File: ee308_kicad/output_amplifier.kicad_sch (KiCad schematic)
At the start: 24 parts, among them Q2 2N3904, Q4 2N3904, Q5 2N3904, Q6 2N3906, Q7 2N3904, Q8 2N3906

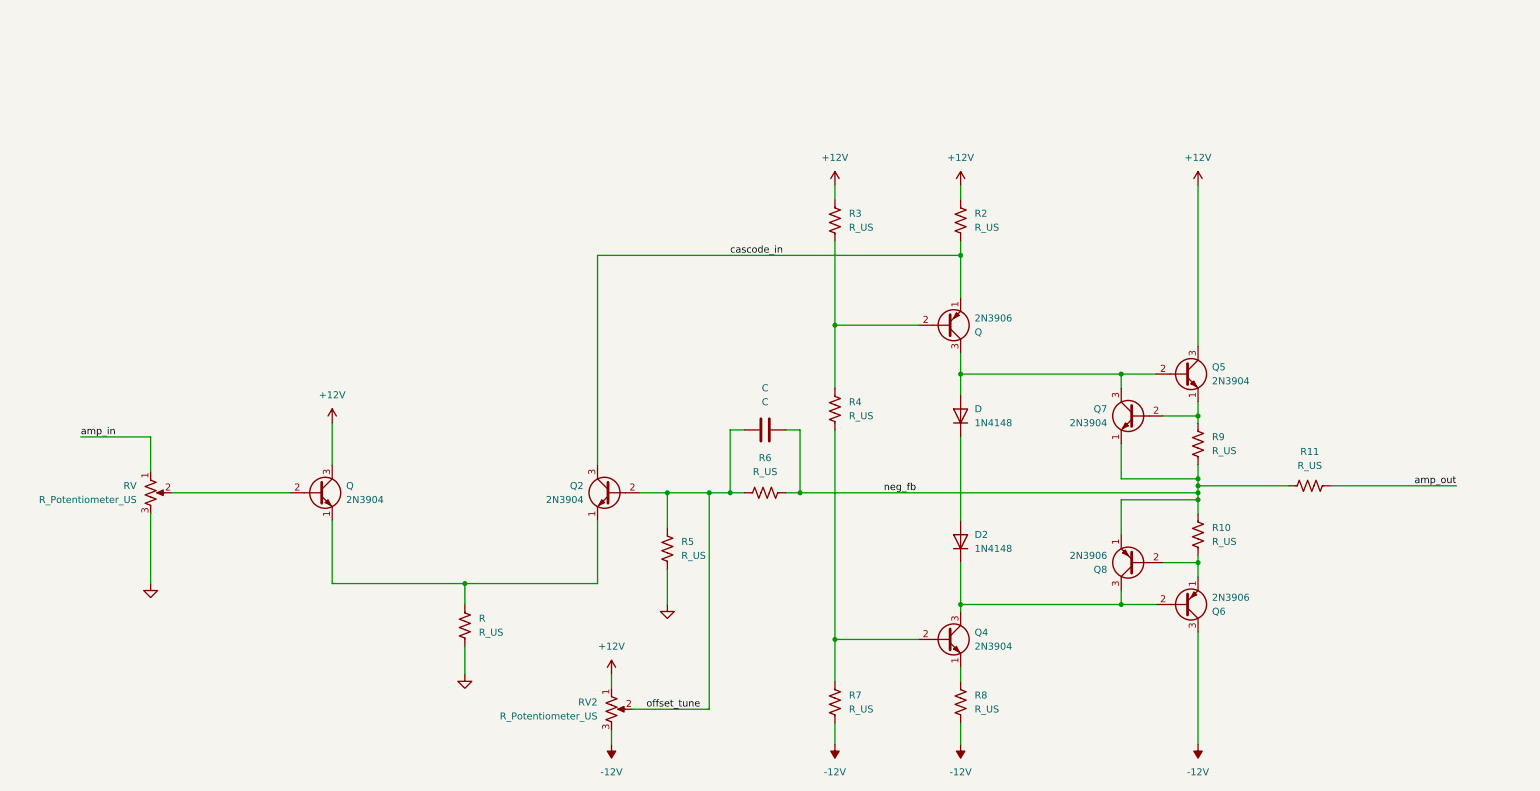
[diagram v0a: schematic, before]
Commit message: Update amplifier sims and kicad schematic.
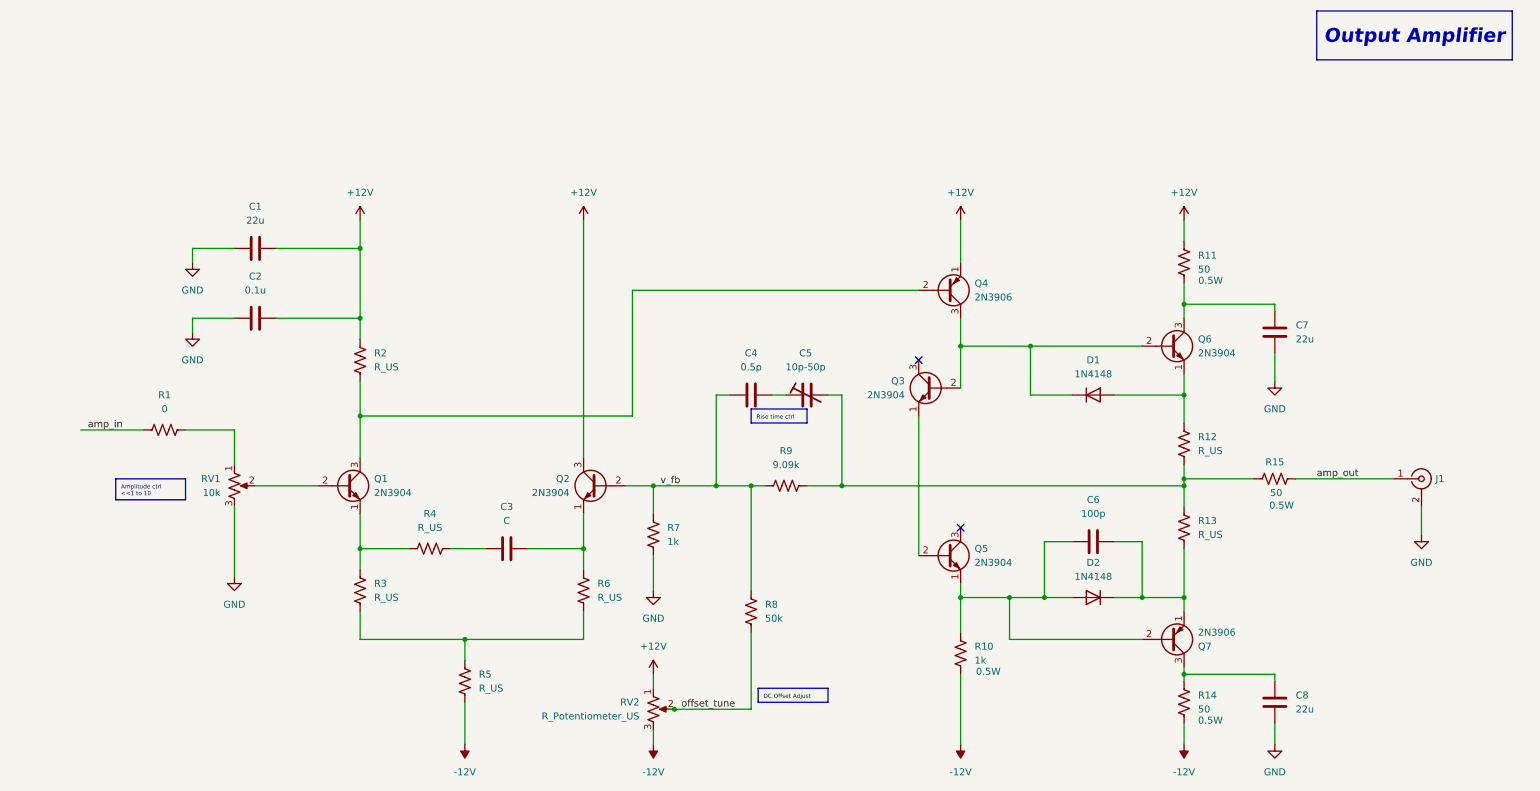
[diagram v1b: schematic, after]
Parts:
- removed C: C, symbol Device:C
- removed Q4, Q7: 2N3904, Package_TO_SOT_THT:TO-92_Inline, symbol Transistor_BJT:2N3904
- removed Q8: 2N3906, Package_TO_SOT_THT:TO-92_Inline, symbol Transistor_BJT:2N3906
- removed R5: R_US, symbol Device:R_US
- added C1, C7, C8: 22u, Capacitor_SMD:C_0805_2012Metric_Pad1.18x1.45mm_HandSolder, symbol Device:C
- added C2: 0.1u, Capacitor_SMD:C_0805_2012Metric_Pad1.18x1.45mm_HandSolder, symbol Device:C
- added C3: C, Capacitor_SMD:C_0805_2012Metric_Pad1.18x1.45mm_HandSolder, symbol Device:C
- added C4: 0.5p, Capacitor_SMD:C_0805_2012Metric_Pad1.18x1.45mm_HandSolder, symbol Device:C
- added C5: 10p-50p, Capacitor_SMD:C_Trimmer_Murata_TZY2, symbol Device:C_Trim
- added C6: 100p, Capacitor_SMD:C_0805_2012Metric_Pad1.18x1.45mm_HandSolder, symbol Device:C
- added J1: Conn_Coaxial, Connector_Coaxial:BNC_TEConnectivity_1478035_Horizontal, symbol Connector:Conn_Coaxial
- added Q3, Q5: 2N3904, Package_TO_SOT_THT:TO-92_Inline, symbol Transistor_BJT:2N3904
- added R1: 0, Resistor_SMD:R_0805_2012Metric_Pad1.20x1.40mm_HandSolder, symbol Device:R_US
- added R12, R13: R_US, Resistor_SMD:R_0805_2012Metric_Pad1.20x1.40mm_HandSolder, symbol Device:R_US
- added R14, R15: 50, Resistor_SMD:R_1206_3216Metric_Pad1.30x1.75mm_HandSolder, symbol Device:R_US
- R10: value R_US -> 1k; footprint (none) -> Resistor_SMD:R_1206_3216Metric_Pad1.30x1.75mm_HandSolder; Power (none) -> 0.5W
- R11: value R_US -> 50; footprint (none) -> Resistor_SMD:R_1206_3216Metric_Pad1.30x1.75mm_HandSolder; Power (none) -> 0.5W
- R2, R3, R4, R6: footprint (none) -> Resistor_SMD:R_0805_2012Metric_Pad1.20x1.40mm_HandSolder
- R7: value R_US -> 1k; footprint (none) -> Resistor_SMD:R_0805_2012Metric_Pad1.20x1.40mm_HandSolder
- R8: value R_US -> 50k; footprint (none) -> Resistor_SMD:R_0805_2012Metric_Pad1.20x1.40mm_HandSolder
- R9: value R_US -> 9.09k; footprint (none) -> Resistor_SMD:R_0805_2012Metric_Pad1.20x1.40mm_HandSolder
- RV1: renamed from RV; value R_Potentiometer_US -> 10k; footprint (none) -> Potentiometer_SMD:Potentiometer_ACP_CA6-VSMD_Vertical
- renumbered D to D1, Q to Q1, Q to Q4, Q5 to Q6, Q6 to Q7, R to R5
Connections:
- net +12V: now also Q2.3 (C), Q4.1 (E), R11.1, C1.2, C2.2; no longer Q1.3 (C), Q6.3 (C), R3.1
- net -12V: now also R10.2, R5.2, R14.2; no longer Q7.3 (C), R7.2, R8.2
- net GND: now also R7.2, C1.1, C2.1, C7.1, C8.1, J1.2 (Ext); no longer R5.2
- net amp_in: now also R1.2; no longer RV1.1
- net amp_out: now also J1.1 (In), R15.2; no longer R11.2
- net offset_tune: now also R8.2; no longer Q2.2 (B), R6.1
- net at D1.1 (K): now also Q4.3 (C), Q6.2 (B), Q3.2 (B); no longer D2.2 (A)
- net at Q7.1 (E): now also D2.1 (K), C6.2, R13.2; no longer R10.2
- net v_fb: now reaches R8.1
- net v_fb: now also Q2.2 (B), R7.1, R9.2, C4.1
- net at Q6.1 (E): now also D1.2 (A), R12.1; no longer R9.1
- net at Q7.2 (B): now also D2.2 (A), R10.1, C6.1, Q5.1 (E); no longer D2.1 (K)
- net at R4.2: now also Q1.1 (E), R3.1; no longer R7.1
- removed net cascode_in: Q2.3 (C), Q4.1 (E), R2.2
- removed net neg_fb: R10.1, R11.1, R6.2, R9.2
- new net: C7.2, Q6.3 (C), R11.2
- new net: C3.1, R4.1
- new net: Q3.1 (E), Q5.2 (B)
- new net: Q1.3 (C), Q4.2 (B), R2.2
- new net: C3.2, Q2.1 (E), R6.1
- new net: R3.2, R5.1, R6.2
- new net: C4.2, C5.1
- new net: C5.2, R12.2, R13.1, R15.1, R9.1
- new net: R1.1, RV1.1
- new net: C8.2, Q7.3 (C), R14.1
- no-connect marks 0 -> 2
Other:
- moved on the sheet: D1, D2, Q1, Q2, Q4, Q6, Q7, R5, RV1, RV2

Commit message: Update amplifier sims and kicad schematic.
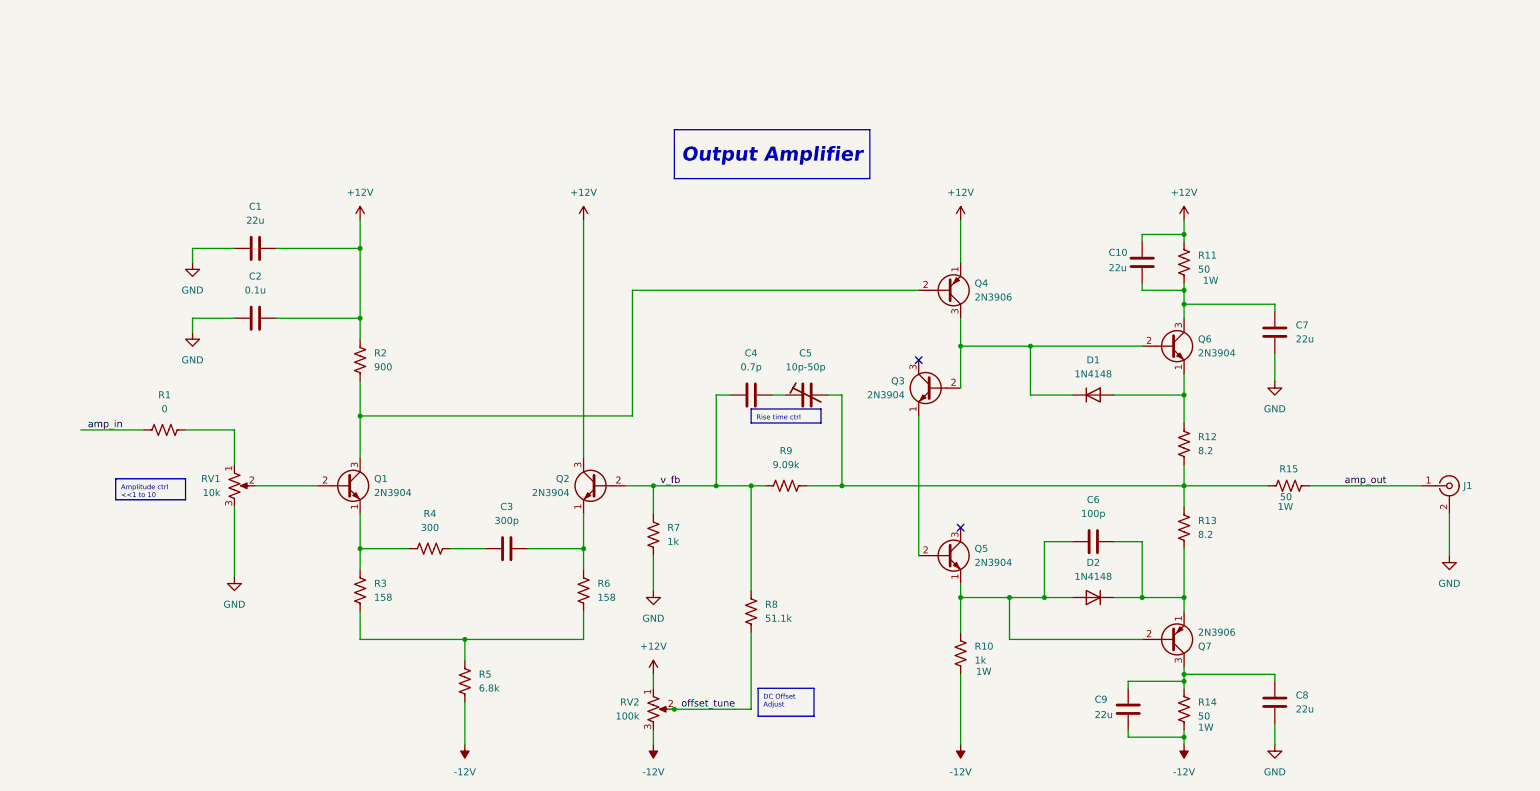
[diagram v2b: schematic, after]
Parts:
- added C10, C9: 22u, Capacitor_SMD:C_0805_2012Metric_Pad1.18x1.45mm_HandSolder, symbol Device:C
- C3: value C -> 300p
- C4: value 0.5p -> 0.7p
- R10, R11, R14, R15: Power 0.5W -> 1W
- R12, R13: value R_US -> 8.2
- R2: value R_US -> 900
- R3, R6: value R_US -> 158
- R4: value R_US -> 300
- R5: value R_US -> 6.8k; footprint (none) -> Resistor_SMD:R_1206_3216Metric_Pad1.30x1.75mm_HandSolder
- R8: value 50k -> 51.1k
- RV2: value R_Potentiometer_US -> 100k
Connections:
- net +12V: now also C10.2
- net -12V: now also C9.1
- net at C7.2, Q6.3 (C), R11.2: now also C10.1
- net at C8.2, Q7.3 (C), R14.1: now also C9.2
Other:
- moved on the sheet: J1, R14, R15

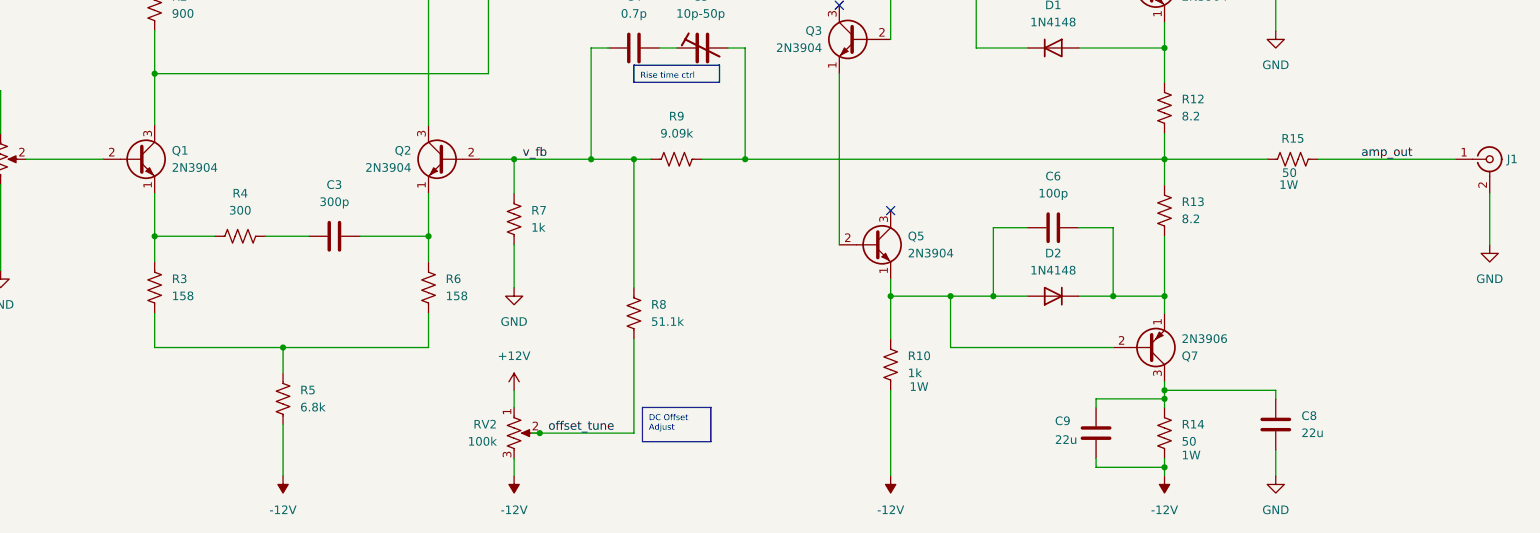
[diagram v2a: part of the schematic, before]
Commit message: Add initial Schmitt trigger simulation with working square wave outputs.
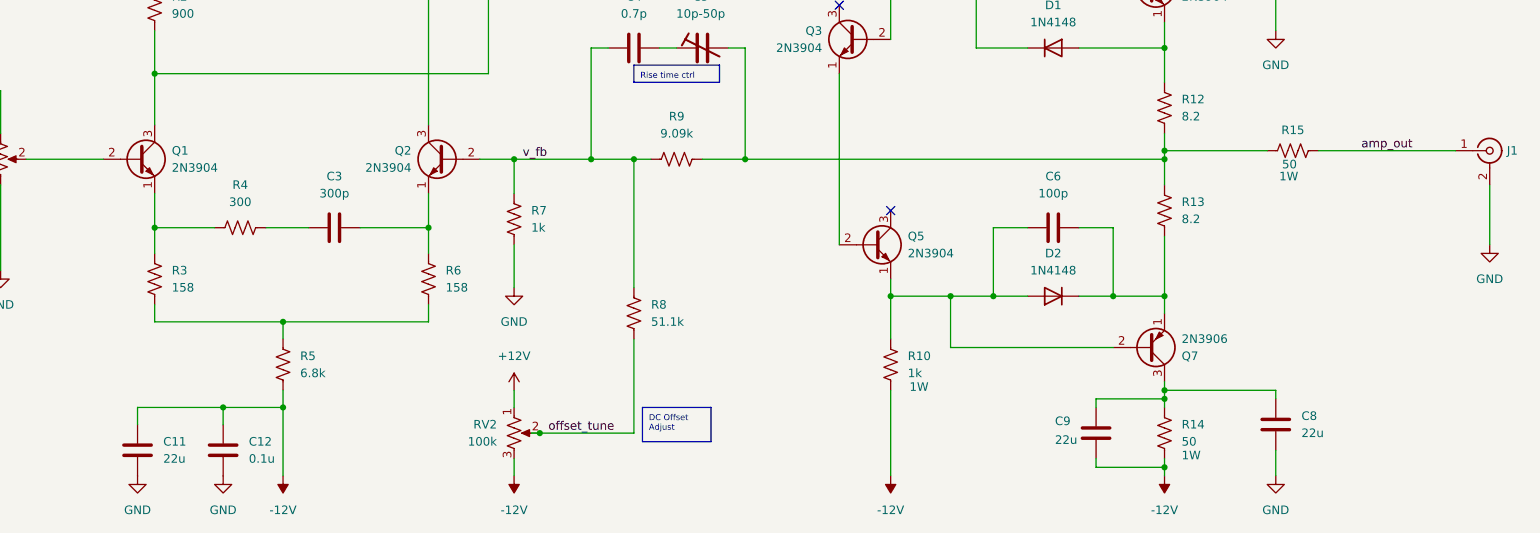
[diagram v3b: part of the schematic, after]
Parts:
- added C11: 22u, Capacitor_SMD:C_0805_2012Metric_Pad1.18x1.45mm_HandSolder, symbol Device:C
- added C12: 0.1u, Capacitor_SMD:C_0805_2012Metric_Pad1.18x1.45mm_HandSolder, symbol Device:C
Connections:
- net -12V: now also C11.2, C12.2
- net GND: now also C11.1, C12.1
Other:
- moved on the sheet: C3, J1, R15, R3, R4, R5, R6
